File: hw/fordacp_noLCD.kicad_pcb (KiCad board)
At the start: 2 copper layers, 53.7 x 28 mm, 33 parts, among them IC1 ATMEGA2560-A, P1 CONN_02X06, U1 SP3485CN, U2 AP1117D50, U3 BLK-MD-SPK-B, U4 XS3860, Y1 16MHz

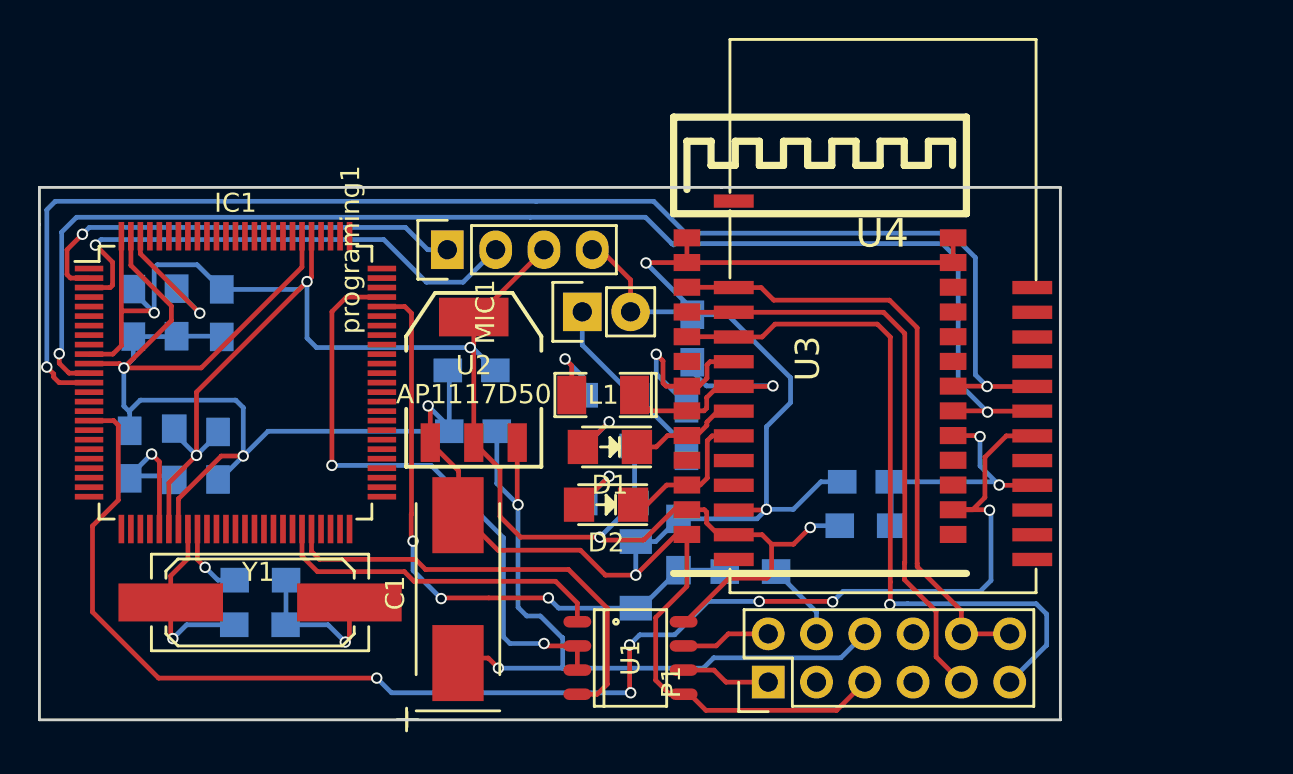
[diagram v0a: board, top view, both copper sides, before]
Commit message: update pcb without LCD
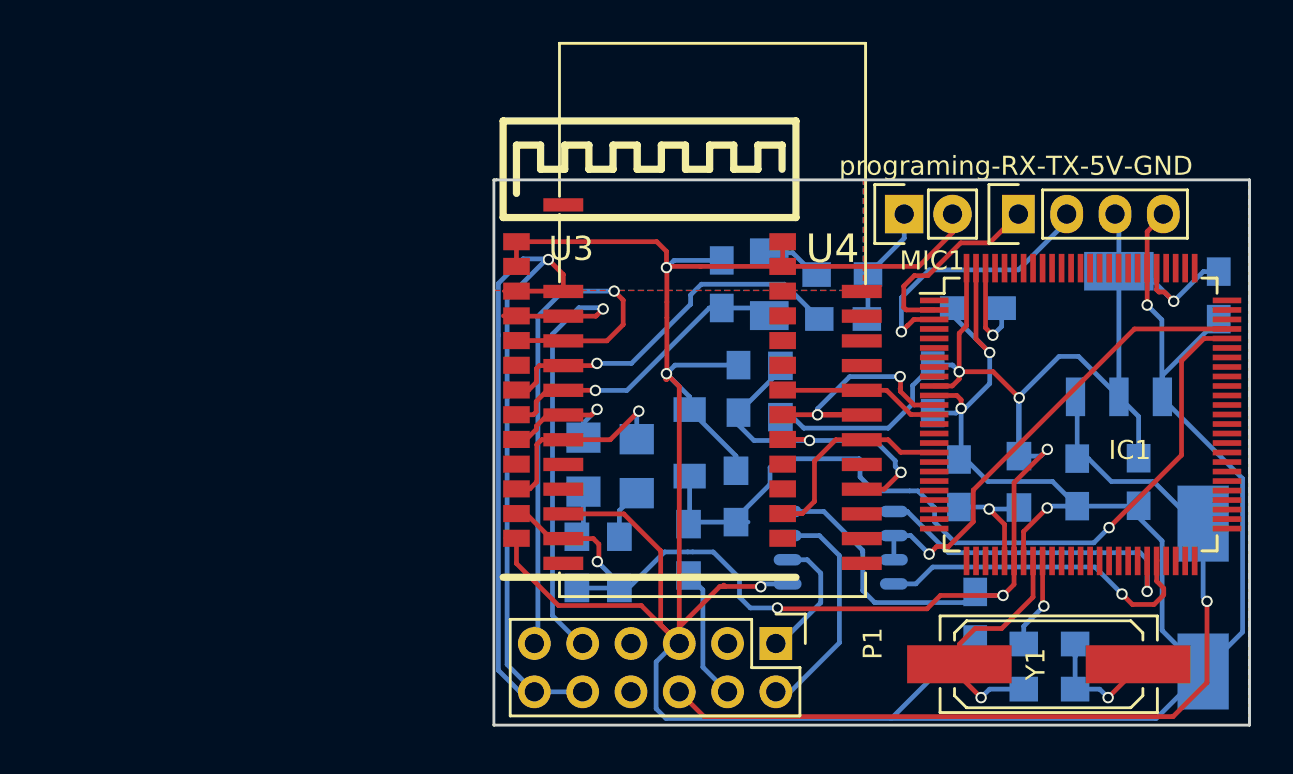
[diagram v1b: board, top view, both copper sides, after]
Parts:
- C1, D1, D2, L1, U1, U2: moved to B.Cu
- moved C8 52.4 mm to (152.8, 94.5)
- moved IC1 44.5 mm to (145.6, 100.7)
- moved R8 44.4 mm to (142.3, 104.3)
- moved C10 43.6 mm to (139.2, 104.3)
- moved C5 42.2 mm to (137.8, 99.4)
- moved C9 42.1 mm to (140.2, 95.1), turned to 180 degrees
- moved R2 41.7 mm to (143.9, 115.2)
- moved R3 41.6 mm to (143.9, 112.8)
- moved Y1 41.6 mm to (143.9, 113.9)
- moved C6 40.7 mm to (140.0, 111.3)
- moved C1 39.2 mm to (152.0, 110.4), turned to 270 degrees
- moved C7 35.6 mm to (148.6, 104.3), turned to 270 degrees
- moved U2 34.0 mm to (147.6, 96.5), turned to 180 degrees
- moved C2 31.9 mm to (145.4, 104.3), turned to 270 degrees
- moved programing-RX-TX-5V-GND 30.1 mm to (142.3, 90.2)
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- renumbered programing1 to programing-RX-TX-5V-GND
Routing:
- net /BT_WAKE: track 77.7 -> 11.1 mm, vias 6 -> 0
- net /BT_RX: track 72.5 -> 8.53 mm, vias 2 -> 0
- net /BT_TX: track 70.1 -> 14.8 mm
- net GND: track 168.7 -> 213.0 mm, vias 6 -> 7
- net GNDA: track 32.6 -> 58.4 mm, vias 0 -> 1
- net /RX0: track 23.5 -> 10.4 mm, vias 1 -> 0
- net +5V: track 107.7 -> 120.0 mm, vias 6 -> 7
- net /TX0: track 26.6 -> 14.5 mm
- net /ENABLE_5V: track 33.6 -> 43.6 mm, vias 3 -> 1
- net /MIC: track 9.90 -> 19.8 mm
- net +12V: track 41.3 -> 49.1 mm, vias 2 -> 1
- net /AUXINR: track 38.2 -> 30.5 mm
- net /RS485-B: track 4.71 -> 12.2 mm
- net /RS485_ENA: track 32.2 -> 25.1 mm, vias 2 -> 1
- net /RS485_DI: track 23.8 -> 17.6 mm, vias 0 -> 1
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- added copper zone on B.Cu, net GND
- added copper zone on F.Cu, net GND
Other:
- board size 53.7 x 28 mm -> 39.7 x 28.7 mm

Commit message: update
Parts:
- removed programing-RX-TX-5V-GND: CONN_01X02, Pin_Headers:Pin_Header_Straight_1x04
- added programing1: CONN_01X05, Pin_Headers:Pin_Header_Straight_1x05, F.Cu at (142.2, 90.2)
- C10, C11: value 2u2/10V -> 1u/16V
- C4: footprint Capacitors_SMD:C_0805_HandSoldering -> Capacitors_SMD:C_1206_HandSoldering
- R8, R9: value 4k7 -> 10k
- moved C4 9.22 mm to (127.5, 103.1), turned to 270 degrees
- moved C3 7.06 mm to (126.6, 98.4)
- moved D3 6.11 mm to (125.0, 108.3), turned to 270 degrees
- moved L1 5.79 mm to (132.0, 98.9), turned to 0 degrees
- moved C11 4.47 mm to (125.0, 103.1), turned to 270 degrees
- moved R7 3.55 mm to (127.3, 108.6), turned to 90 degrees
- moved R9 3.41 mm to (129.9, 102.9)
- moved R1 3.31 mm to (131.8, 96.5), turned to 0 degrees
- moved R6 2.35 mm to (122.7, 108.5)
- moved C9 2.12 mm to (139.3, 93.2)
- moved R4 0.97 mm to (118.1, 108.5)
- moved R5 0.92 mm to (120.4, 108.5)
- moved U1 0.66 mm to (133.0, 108.4)
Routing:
- net GNDA: track 58.4 -> 32.8 mm
- net /ARD_RESET: track 6.30 -> 22.4 mm, vias 1 -> 2
- net /MIC: track 19.8 -> 10.6 mm
- net +5V: track 120.0 -> 113.3 mm
- net Net-(C3-Pad1): track 6.33 -> 12.9 mm
- net GND: track 213.0 -> 219.4 mm, vias 7 -> 6
- net /ENABLE_5V: track 43.6 -> 40.4 mm
- net /BT_TX: track 14.8 -> 12.0 mm
- net /AUXINL: track 25.8 -> 28.2 mm
- net /RS485_ENA: track 25.1 -> 27.2 mm
- net /MIC_BIAS: track 16.1 -> 18.0 mm
- net /ARD_AREF: track 5.30 -> 3.41 mm
- net /AUXINR: track 30.5 -> 32.3 mm
- net /ENABLE: track 6.97 -> 8.38 mm
- net /RX0: track 10.4 -> 11.8 mm
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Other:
- board text added: "5V"
- board text added: "BLK-MD-SPK-B"
- board text added: "GND"
- board text added: "MIC"
- board text added: "RX"
- board text added: "TX"
- board text added: "XS3860"

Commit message: added SPI interface
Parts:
- added P2: CONN_02X03, Pin_Headers:Pin_Header_Straight_2x03, F.Cu at (132.2, 115.3)
- R1: value 2k7 -> 2k7(3k3)
- moved Y1 2.44 mm to (146.3, 113.8)
- moved C6 0.77 mm to (139.8, 110.6), turned to 180 degrees
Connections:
- IC1 pad 20: (no net) -> /SCK
- IC1 pad 21: (no net) -> /MOSI
- IC1 pad 22: (no net) -> /MISO
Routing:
- net /SCK: track 0.00 -> 15.2 mm, vias 0 -> 1
- net /MISO: track 0.00 -> 14.4 mm
- net /MOSI: track 0.00 -> 9.97 mm
- net /ARD_RESET: track 22.4 -> 31.3 mm
- net +12V: track 49.1 -> 52.6 mm
- net +5V: track 113.3 -> 116.3 mm
- net GND: track 219.4 -> 221.7 mm
- net Net-(R2-Pad2): track 6.79 -> 8.94 mm
- net /RS485_ENA: track 27.2 -> 26.6 mm
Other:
- board text added: "RADIO"
- board text added: "RST"
- board text added: "SPI"

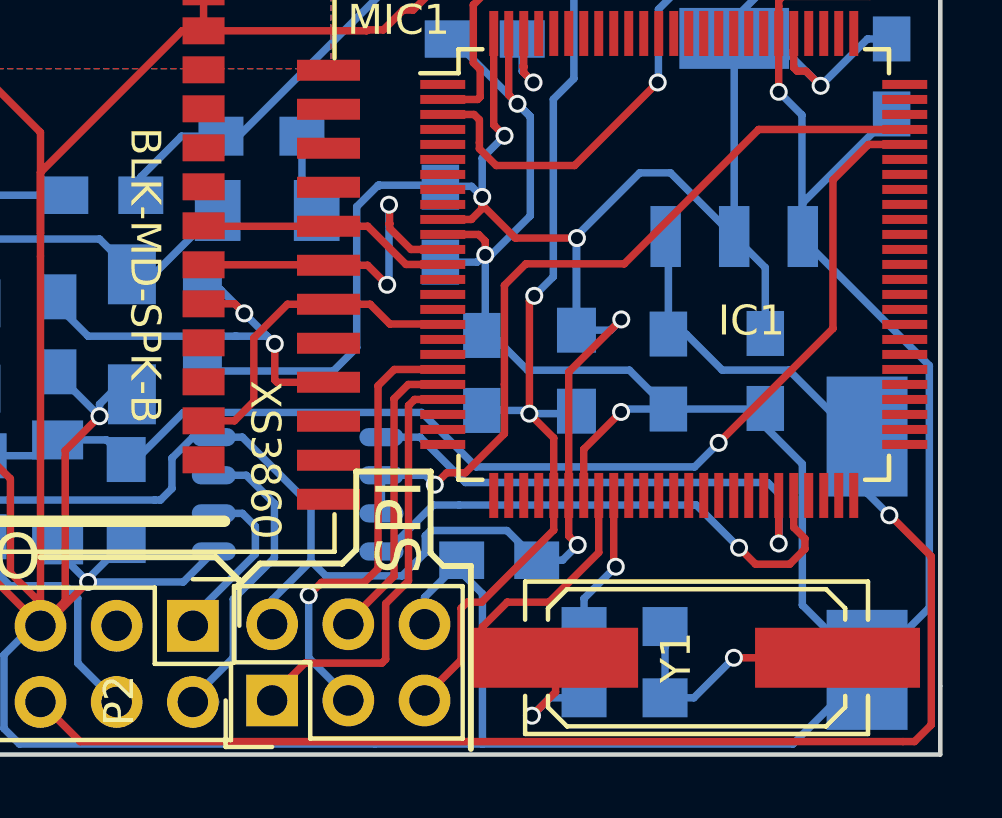
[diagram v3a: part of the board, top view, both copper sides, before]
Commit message: L1 better housing
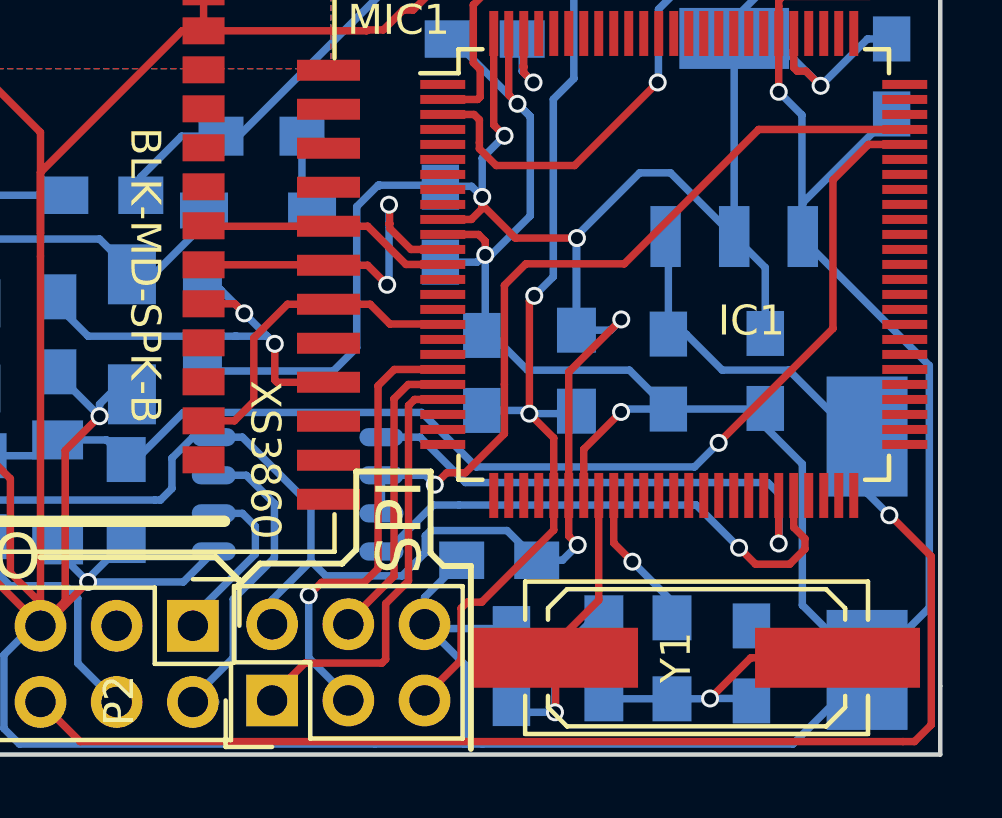
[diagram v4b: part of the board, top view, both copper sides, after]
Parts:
- added C12: 22, Capacitors_SMD:C_0805_HandSoldering, B.Cu at (140.2, 114.1)
- added C13: 22, Capacitors_SMD:C_0805_HandSoldering, B.Cu at (148.2, 114.0)
- L1: footprint SMD_Packages:SMD-1206_Pol -> Choke_SMD:Choke_SMD_1206_Standard
- moved R3 1.90 mm to (145.5, 113.9), turned to 270 degrees
- moved R2 1.49 mm to (143.2, 113.9), turned to 270 degrees
- moved L1 0.30 mm to (131.7, 98.9)
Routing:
- net GND: track 221.7 -> 227.8 mm
- net Net-(C13-Pad1): track 8.94 -> 10.4 mm
- net Net-(C12-Pad1): track 12.7 -> 14.0 mm
